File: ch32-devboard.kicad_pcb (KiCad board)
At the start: 2 copper layers, 40.5 x 50 mm, 8 parts, among them J1 USB_C_Receptacle_USB2.0_16P, J2 Conn_01x10_Pin, J3 Conn_01x10_Pin, J4 Conn_01x03_Socket, J5 Conn_01x05_Pin

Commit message: add leds,decouple vdd, resistory for d+ d-
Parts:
- added C1: C_Small, Capacitor_SMD:C_0805_2012Metric_Pad1.18x1.45mm_HandSolder, F.Cu at (146.5, 91.0)
- added D1: LED, LED_SMD:LED_0805_2012Metric_Pad1.15x1.40mm_HandSolder, F.Cu at (132.0, 71.5)
- added D2: LED, LED_SMD:LED_0805_2012Metric_Pad1.15x1.40mm_HandSolder, F.Cu at (140.5, 76.5)
- added R3: R_Small, Resistor_SMD:R_0805_2012Metric_Pad1.20x1.40mm_HandSolder, F.Cu at (132.0, 67.0)
- added R4: R_Small, Resistor_SMD:R_0805_2012Metric_Pad1.20x1.40mm_HandSolder, F.Cu at (144.5, 76.5)
- added R5: R_Small, Resistor_SMD:R_0805_2012Metric_Pad1.20x1.40mm_HandSolder, F.Cu at (148.0, 77.5)
- added R6: R_Small, Resistor_SMD:R_0805_2012Metric_Pad1.20x1.40mm_HandSolder, F.Cu at (152.5, 73.0)
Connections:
- J1 pad A6: /PC17 -> /UD+
- J1 pad A7: /PC16 -> /UD-
- J1 pad B6: /PC17 -> /UD+
- J1 pad B7: /PC16 -> /UD-
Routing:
- net /UD-: track 0.00 -> 17.3 mm
- net Net-(J1-SBU2): track 0.00 -> 17.2 mm, vias 0 -> 2
- net /PC16: track 33.0 -> 17.5 mm
- net Net-(J1-SBU1): track 0.00 -> 13.4 mm, vias 0 -> 2
- net /PC17: track 37.0 -> 25.4 mm
- net Net-(J1-CC1): track 0.00 -> 9.88 mm
- net Net-(J1-CC2): track 0.00 -> 9.66 mm, vias 0 -> 2
- net /UD+: track 0.00 -> 9.37 mm
- net /VDD: track 61.7 -> 69.4 mm
- net /PA6: track 11.9 -> 16.1 mm
- net Net-(D1-K): track 0.00 -> 2.45 mm
- net Net-(D2-K): track 0.00 -> 1.95 mm
- net GND: vias 5 -> 8

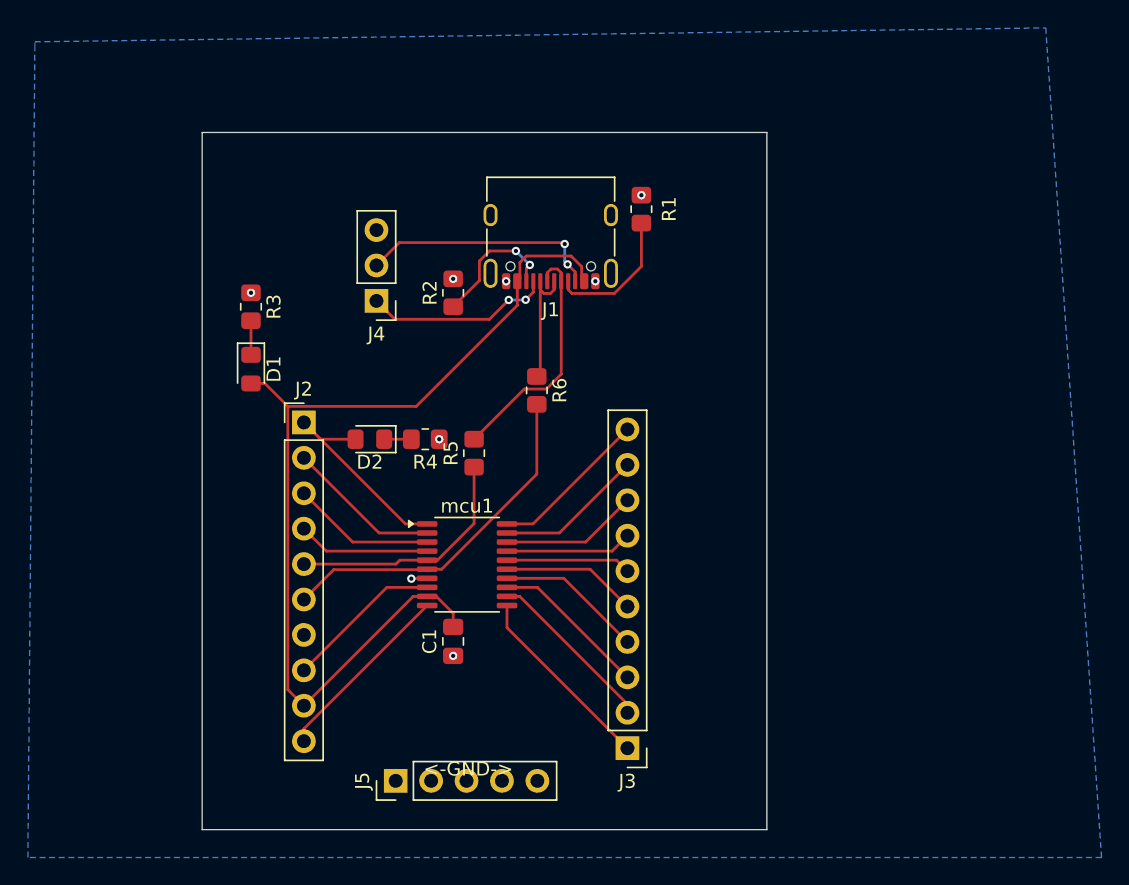
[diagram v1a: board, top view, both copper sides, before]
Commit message: complete with ch32x033
no proper button footprint
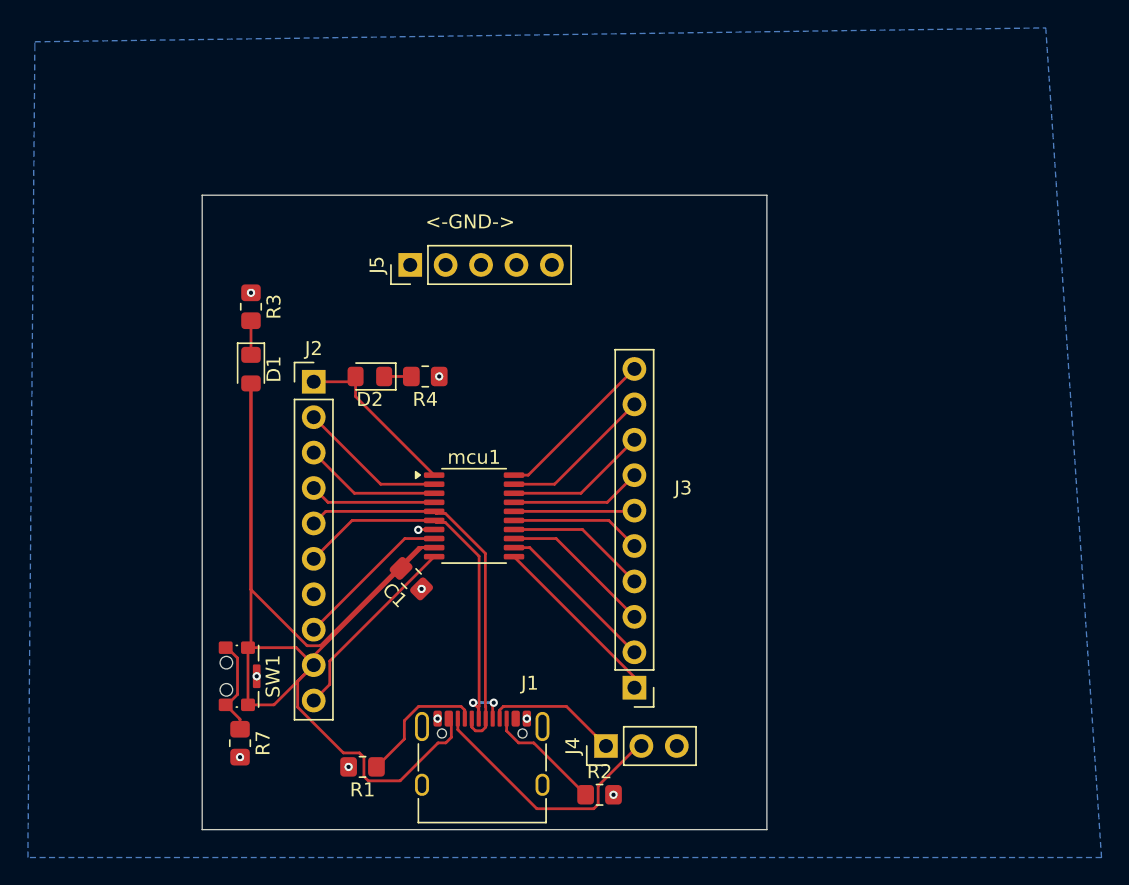
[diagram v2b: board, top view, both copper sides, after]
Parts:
- removed R5, R6: R_Small, Resistor_SMD:R_0805_2012Metric_Pad1.20x1.40mm_HandSolder
- added R7: R, Resistor_SMD:R_0805_2012Metric_Pad1.20x1.40mm_HandSolder, F.Cu at (131.2, 98.3)
- added SW1: CK_KMS2xxG, Button_Switch_SMD:SW_SPST_CK_KMS2xxGP, F.Cu at (131.0, 93.5)
- moved R1 44.7 mm to (140.0, 100.0), turned to 180 degrees
- moved J1 39.0 mm to (148.6, 100.2), turned to 0 degrees
- moved R2 37.5 mm to (157.0, 102.0), turned to 0 degrees
- moved J5 37.0 mm to (143.4, 64.0)
- moved J4 35.9 mm to (157.5, 98.5), turned to 90 degrees
- moved C1 5.41 mm to (143.5, 86.5), turned to 135 degrees
- moved D2 4.50 mm to (140.5, 72.0)
- moved R4 4.50 mm to (144.5, 72.0)
- moved J3 4.37 mm to (159.5, 94.3)
- moved mcu1 3.54 mm to (148.0, 82.0)
- moved J2 3.00 mm to (136.5, 72.4)
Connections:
- J1 pad A6: /UD+ -> /PC17
- J1 pad A7: /UD- -> /PC16
- J1 pad B6: /UD+ -> /PC17
- J1 pad B7: /UD- -> /PC16
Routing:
- net /VDD: track 69.4 -> 99.5 mm
- net /UD-: track 17.3 -> 0.00 mm
- net /PC16: track 17.5 -> 28.2 mm
- net /UD+: track 9.37 -> 0.00 mm
- net Net-(R7-Pad1): track 0.00 -> 7.11 mm
- net /PC17: track 25.4 -> 29.7 mm, vias 0 -> 2
- net /PA6: track 16.1 -> 12.0 mm
- net Net-(J1-SBU1): track 13.4 -> 9.52 mm, vias 2 -> 0
- net Net-(J1-SBU2): track 17.2 -> 18.7 mm, vias 2 -> 0
- net Net-(J1-CC2): track 9.66 -> 8.44 mm, vias 2 -> 0
- net /PA11: track 13.8 -> 13.0 mm
- net /PA10: track 12.5 -> 11.7 mm
- net /PA9: track 13.4 -> 13.9 mm
- net GND: vias 8 -> 10
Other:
- board size 40.5 x 50 mm -> 40.5 x 45.5 mm

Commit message: add ldo, change button footprint, reroute and compact, label pins
give value to resistors and capacitors, remove series resistor from usb line, correct reset button pullup resistor from pulldown
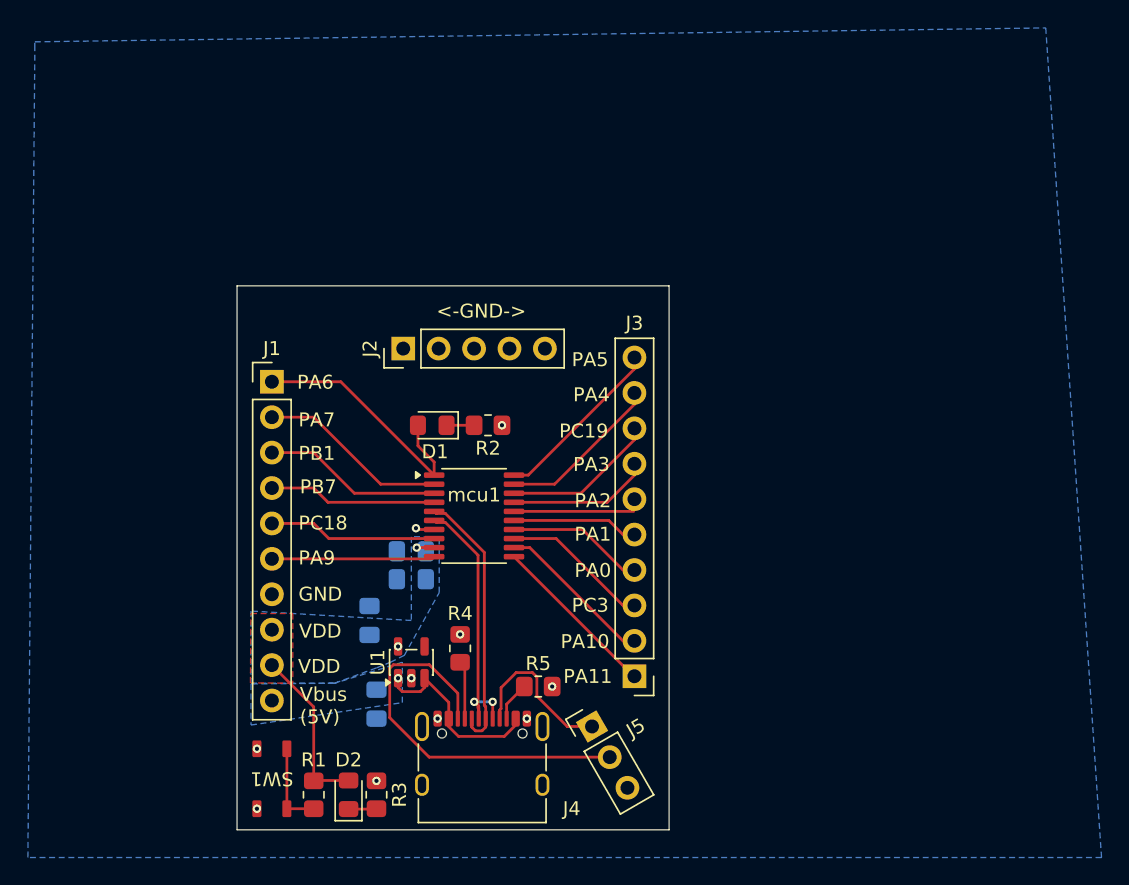
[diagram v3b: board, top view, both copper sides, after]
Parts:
- removed the R1 at (140.0, 100.0)
- added C1: 0.1uF, Capacitor_SMD:C_0805_2012Metric_Pad1.18x1.45mm_HandSolder, B.Cu at (143.5, 84.5)
- added C3: 4.7uF, Capacitor_SMD:C_0805_2012Metric_Pad1.18x1.45mm_HandSolder, B.Cu at (140.5, 89.5)
- added C4: 4.7uF, Capacitor_SMD:C_0805_2012Metric_Pad1.18x1.45mm_HandSolder, B.Cu at (141.0, 95.5)
- added R4: 5.1k, Resistor_SMD:R_0805_2012Metric_Pad1.20x1.40mm_HandSolder, F.Cu at (147.0, 91.5)
- added U1: AP2112K-3.3, Package_TO_SOT_SMD:SOT-23-5, F.Cu at (143.5, 92.5)
- C2: renamed from C1; value C_Small -> 1uF; moved to B.Cu
- R1: renamed from R7; value R -> 10k
- R2: renamed from R4; value R_Small -> 1k
- R3: value R_Small -> 1k
- R5: renamed from R2; value R_Small -> 5.1k
- SW1: footprint Button_Switch_SMD:SW_SPST_CK_KMS2xxGP -> CH32-devBoard:smd-push-button-TS3425PA
- moved R3 36.1 mm to (141.0, 102.0)
- moved D2 31.3 mm to (139.0, 102.0), turned to 90 degrees
- moved R5 8.92 mm to (152.6, 94.2)
- moved SW1 7.77 mm to (133.5, 100.8), turned to 180 degrees
- moved R1 6.45 mm to (136.5, 102.0), turned to 90 degrees
- moved J2 6.02 mm to (142.9, 70.0)
- moved R2 5.70 mm to (149.0, 75.5)
- moved D1 5.68 mm to (145.0, 75.5)
- moved J1 3.00 mm to (133.5, 72.4)
- moved J5 1.72 mm to (156.5, 97.1), turned to 30 degrees
- moved J3 0.82 mm to (159.5, 93.5)
- turned C2 to 0 degrees
- renumbered D2 to D1, D1 to D2, J2 to J1, J5 to J2, J1 to J4, J4 to J5
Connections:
- J1 pad 10: /PA9 -> /Vbus
- J1 pad 5: /PC16 -> /PC18
- J1 pad 6: /PC17 -> /PA9
- J1 pad 8: /PC18 -> /VDD
- J4 pad A4: /VDD -> /Vbus
- J4 pad A6: /PC17 -> /UD+
- J4 pad A7: /PC16 -> /UD-
- J4 pad A9: /VDD -> /Vbus
- J4 pad B4: /VDD -> /Vbus
- J4 pad B6: /PC17 -> /UD+
- J4 pad B7: /PC16 -> /UD-
- J4 pad B9: /VDD -> /Vbus
- R1 pad 1: Net-(R7-Pad1) -> Net-(R1-Pad1)
- R1 pad 2: GND -> /VDD
- SW1 pad 1: /VDD -> Net-(R1-Pad1)
- SW1 pad 2: Net-(R7-Pad1) -> GND
- mcu1 pad 5: /PC16 -> /UD-
- mcu1 pad 6: /PC17 -> /UD+
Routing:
- net /VDD: track 99.5 -> 14.4 mm, vias 0 -> 2
- net /PC17: track 29.7 -> 0.00 mm, vias 2 -> 0
- net /PC16: track 28.2 -> 0.00 mm
- net /UD+: track 0.00 -> 19.8 mm, vias 0 -> 2
- net /UD-: track 0.00 -> 19.2 mm
- net /Vbus: track 0.00 -> 13.1 mm, vias 0 -> 1
- net Net-(J4-SBU2): track 18.7 -> 28.1 mm
- net Net-(R7-Pad1): track 7.11 -> 0.00 mm
- net /PA6: track 12.0 -> 18.5 mm
- net Net-(R1-Pad1): track 0.00 -> 6.23 mm
- net Net-(J4-CC2): track 8.44 -> 2.83 mm
- net Net-(J4-CC1): track 9.62 -> 4.18 mm
- net /PB7: track 9.06 -> 12.1 mm
- net /PB1: track 9.84 -> 12.8 mm
- net /PA7: track 10.6 -> 13.6 mm
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- added copper zone on B.Cu, net /VDD
- added copper zone on F.Cu, net /VDD
- added copper zone on B.Cu, net /Vbus
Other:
- board size 40.5 x 45.5 mm -> 31 x 39 mm
- board text added: "Designed in: Param Makers Adda"
- board text added: "GND"
- board text added: "PA0"
- board text added: "PA1"
- board text added: "PA10"
- board text added: "PA11"
- board text added: "PA2"
- board text added: "PA3"
- board text added: "PA4"
- board text added: "PA5"
- board text added: "PA6"
- board text added: "PA7"
- board text added: "PA9"
- board text added: "PB1"
- board text added: "PB7"
- board text added: "PC18"
- board text added: "PC19"
- board text added: "PC3"
- board text added: "VDD"
- board text added: "Vbus (5V)"
- board text added: "license: CERN-OHL-W V2.0"

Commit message: clean Vdd fill
add license notice in pcb routing page, genarate routing PDF with border
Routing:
- net /VDD: track 14.4 -> 47.2 mm
- net /Vbus: track 13.1 -> 22.8 mm
- removed copper zone on B.Cu, net /Vbus

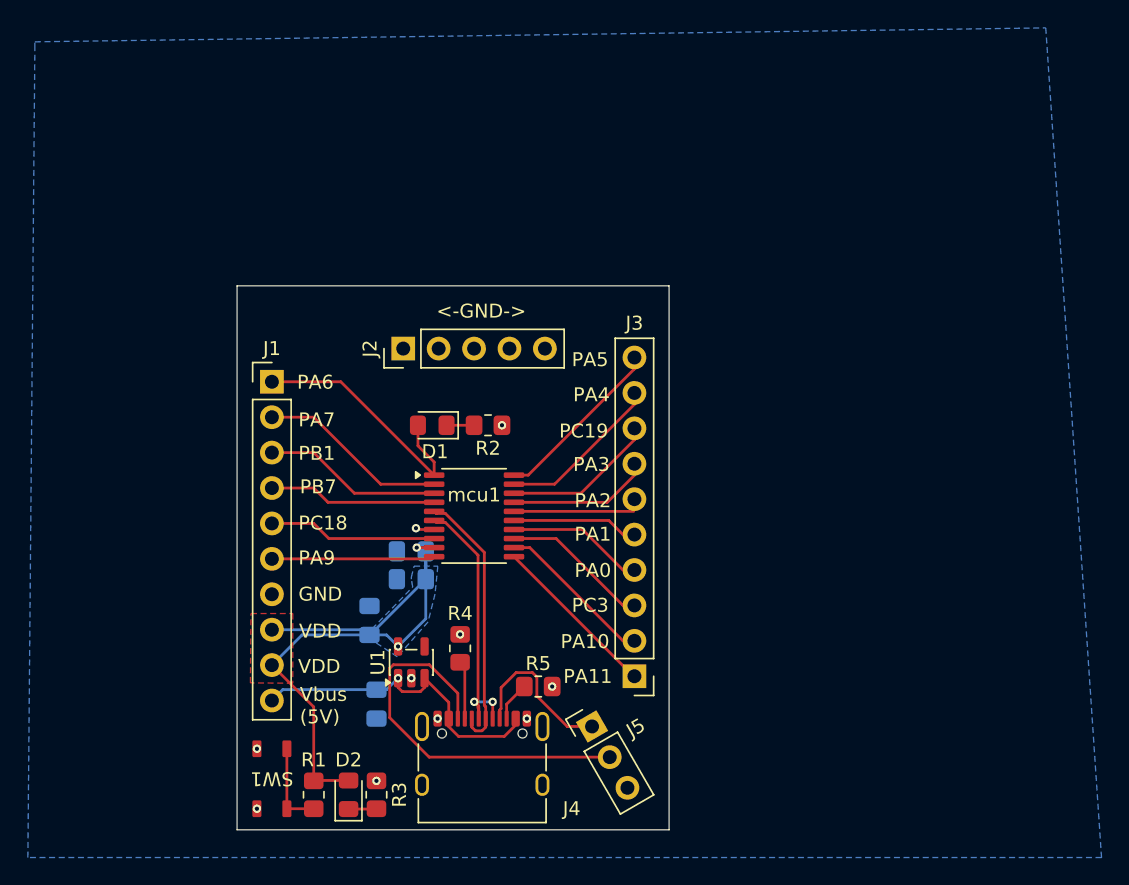
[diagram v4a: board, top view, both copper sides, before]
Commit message: connect reset button to mcu, compact reroute
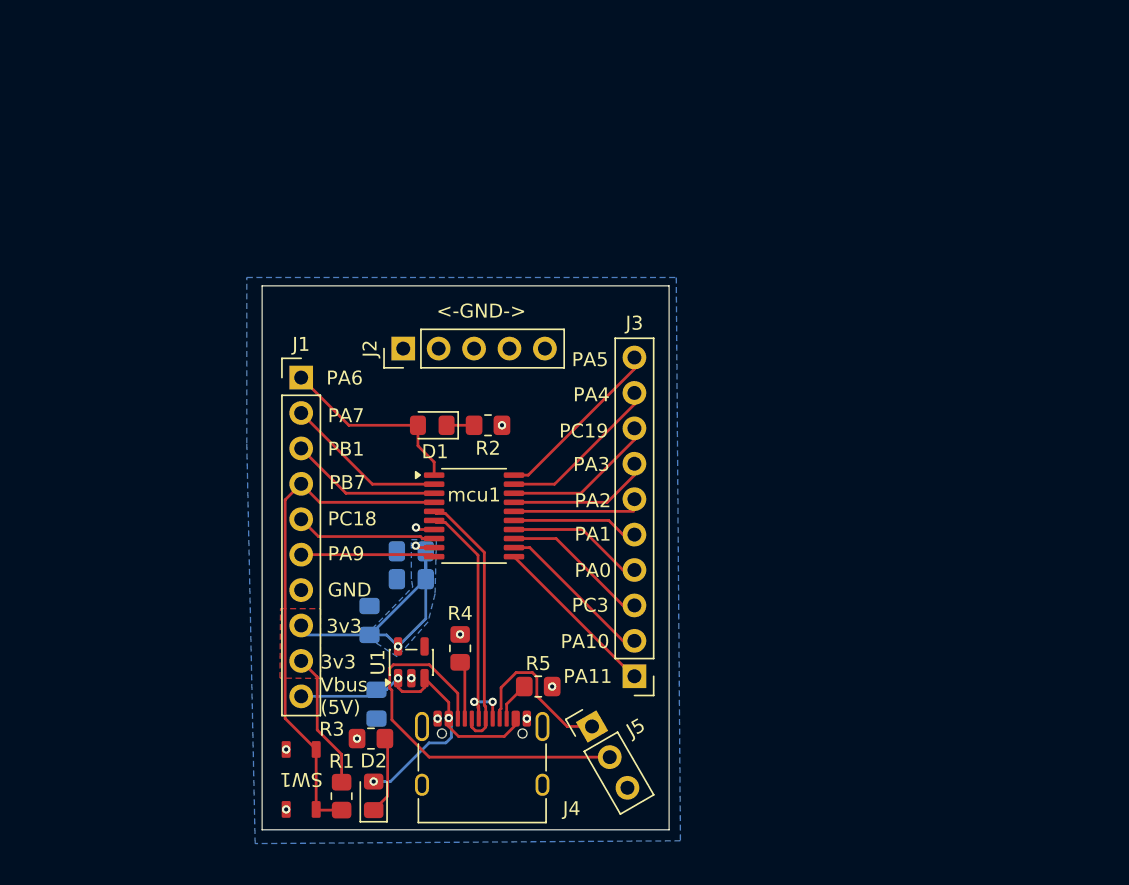
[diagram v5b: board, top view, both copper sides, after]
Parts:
- moved R3 4.05 mm to (140.6, 98.0), turned to 0 degrees
- moved J1 2.12 mm to (135.6, 72.1)
- moved SW1 2.10 mm to (135.6, 100.9)
- moved R1 2.00 mm to (138.5, 102.1)
- moved D2 1.80 mm to (140.8, 102.1)
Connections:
- D2 pad 2: /VDD -> /Vbus
- R1 pad 1: Net-(R1-Pad1) -> /PB7
- SW1 pad 1: Net-(R1-Pad1) -> /PB7
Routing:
- net /PB7: track 12.1 -> 36.7 mm
- net /VDD: track 47.2 -> 34.9 mm
- net Net-(R1-Pad1): track 6.23 -> 0.00 mm
- net /Vbus: track 22.8 -> 28.2 mm, vias 1 -> 3
- net /PA6: track 18.5 -> 13.8 mm
- net Net-(D2-K): track 2.01 -> 5.63 mm
- net /PA9: track 11.7 -> 9.60 mm
- net /PB1: track 12.8 -> 10.9 mm
- net /PA7: track 13.6 -> 11.7 mm
- net /PC18: track 12.1 -> 10.1 mm
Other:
- board size 31 x 39 mm -> 29.2 x 39 mm
- board text added: "3v3"
- board text removed: "VDD"

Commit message: move Vdd pour to F.Cu, connect gnd to shell with trace
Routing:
- net /VDD: track 34.9 -> 14.2 mm, vias 2 -> 3
- net GND: track 1.36 -> 4.07 mm
- added copper zone on F.Cu, net /Vbus
- removed copper zone on B.Cu, net /VDD
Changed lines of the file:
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@@
 		(at 135.6 100.9 180)
 		(property "Reference" "SW1"
-			(at 0 0 180)
+			(at 0 0 0)
 			(unlocked yes)
 			(layer "F.SilkS")
@@
 	)
 	(segment
+		(start 144.830092 96.539102)
+		(end 144.265092 97.104102)
+		(width 0.2)
+		(layer "B.Cu")
+		(net "GND")
+	)
+	(segment
+		(start 145.385092 96.539102)
+		(end 144.830092 96.539102)
+		(width 0.2)
+		(layer "B.Cu")
+		(net "GND")
+	)
+	(segment
+		(start 151.785092 96.539102)
+		(end 152.340092 96.539102)
+		(width 0.2)
+		(layer "B.Cu")
+		(net "GND")
+	)
+	(segment
+		(start 152.340092 96.539102)
+		(end 152.905092 97.104102)
+		(width 0.2)
+		(layer "B.Cu")
+		(net "GND")
+	)
+	(segment
+		(start 145.1375 84.275)
+		(end 146.475 84.275)
+		(width 0.2)
+		(layer "F.Cu")
+		(net "/VDD")
+	)
+	(segment
 		(start 143.95894 84.275)
 		(end 143.818289 84.134349)
@@
 	)
 	(segment
+		(start 146.475 84.275)
+		(end 146.6 84.4)
+		(width 0.2)
+		(layer "F.Cu")
+		(net "/VDD")
+	)
+	(segment
 		(start 136.75 97.35)
 		(end 136.75 93.55)
@@
 	)
 	(via
-		(at 143.818289 84.134349)
+		(at 140.5 90.5375)
 		(size 0.6)
 		(drill 0.3)
@@
 	)
 	(via
-		(at 142.55 91.3625)
+		(at 143.818289 84.134349)
 		(size 0.6)
 		(drill 0.3)
@@
 		(net "/VDD")
 	)
-	(segment
-		(start 144.131849 84.134349)
-		(end 143.818289 84.134349)
-		(width 0.2)
-		(layer "B.Cu")
+	(via
+		(at 144.5375 86.54)
+		(size 0.6)
+		(drill 0.3)
+		(layers "F.Cu" "B.Cu")
 		(net "/VDD")
 	)
@@
 	)
 	(segment
-		(start 144.5375 89.375)
-		(end 142.55 91.3625)
-		(width 0.2)
-		(layer "B.Cu")
-		(net "/VDD")
-	)
-	(segment
-		(start 144.5375 84.54)
-		(end 144.5375 86.54)
-		(width 0.2)
-		(layer "B.Cu")
-		(net "/VDD")
-	)
-	(segment
-		(start 141.725 90.5375)
-		(end 142.55 91.3625)
+		(start 143.818289 84.134349)
+		(end 144.131849 84.134349)
 		(width 0.2)
 		(layer "B.Cu")
@@
 	)
 	(segment
-		(start 140.5 90.5375)
-		(end 141.725 90.5375)
-		(width 0.2)
-		(layer "B.Cu")
-		(net "/VDD")
-	)
-	(segment
-		(start 144.2725 84.275)
-		(end 144.131849 84.134349)
-		(width 0.2)
-		(layer "B.Cu")
-		(net "/VDD")
-	)
-	(segment
-		(start 144.5375 84.54)
-		(end 144.5375 89.375)
-		(width 0.2)
-		(layer "B.Cu")
-		(net "/VDD")
-	)
-	(segment
-		(start 140.54 90.5375)
-		(end 144.5375 86.54)
-		(width 0.2)
-		(layer "B.Cu")
-		(net "/VDD")
-	)
-	(segment
-		(start 140.5 90.5375)
-		(end 135.6625 90.5375)
+		(start 144.131849 84.134349)
+		(end 144.5375 84.54)
 		(width 0.2)
 		(layer "B.Cu")
@@
 	)
 	(zone
-		(net "/VDD")
+		(net "/Vbus")
 		(layer "F.Cu")
-		(name "Vbus")
+		(name "Vbus_1")
 		(hatch edge 0.5)
-		(priority 2)
+		(priority 3)
 		(connect_pads
 			(clearance 0.5)
@@
 		(polygon
 			(pts
-				(xy 134.119618 88.652717) (xy 137 88.652717) (xy 137 93.655728) (xy 134.0797 93.632318)
+				(xy 141.8 92.4) (xy 145.6 92.5) (xy 152.394937 94.970886) (xy 152 99.2) (xy 144.4 99.3) (xy 143.1 98.9)
+				(xy 141.9 96.7) (xy 141.7 94.6)
 			)
 		)
@@
 	(zone
 		(net "/VDD")
-		(layer "B.Cu")
-		(name "vdd")
+		(layer "F.Cu")
+		(name "vdd_1")
 		(hatch edge 0.5)
-		(priority 1)
+		(priority 4)
 		(connect_pads
 			(clearance 0.5)
@@
 		(polygon
 			(pts
-				(xy 143.5 83.7) (xy 145.3 83.7) (xy 145.2 87.6) (xy 144.7 89.6) (xy 142.5 92.1) (xy 140.2 90.6)
-				(xy 143.6 87.1) (xy 143.5 86.54) (xy 143.5 86.4)
+				(xy 134.5 93.9) (xy 134.3 88.9) (xy 143.347885 82.671831) (xy 147.2 82.8) (xy 145.4 92.5) (xy 143.4 92.5)
 			)
 		)
